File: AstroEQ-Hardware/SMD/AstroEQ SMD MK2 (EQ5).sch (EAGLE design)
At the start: 41 parts, among them IC1 ATMEGA162-16AU, IC2 PIC18F14K50-I/SS, IC3 78L05, J1 POWER_JACKPANEL, M1 Motor Driver, M2 Motor Driver, SW1 SWITCH, X1 16MHz, X2 12MHz

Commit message: Correct Board-Schematic Inconsistencies
In the SMD design, the board and schematic files in Eagle had become
inconsistent. This has been corrected.
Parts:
- R15: device SmartPrj:R-EU_R0603 -> rcl:R-EU_R0603
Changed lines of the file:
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@@
 <?xml version="1.0" encoding="utf-8"?>
 <!DOCTYPE eagle SYSTEM "eagle.dtd">
-<eagle version="6.2">
+<eagle version="6.6.0">
 <drawing>
 <settings>
@@
 <grid distance="0.1" unitdist="inch" unit="inch" style="lines" multiple="1" display="no" altdistance="0.01" altunitdist="inch" altunit="inch"/>
 <layers>
-<layer number="1" name="Top" color="4" fill="1" visible="no" active="no"/>
-<layer number="2" name="Route2" color="1" fill="3" visible="no" active="no"/>
-<layer number="3" name="Route3" color="4" fill="3" visible="no" active="no"/>
-<layer number="14" name="Route14" color="1" fill="6" visible="no" active="no"/>
-<layer number="15" name="Route15" color="4" fill="6" visible="no" active="no"/>
-<layer number="16" name="Bottom" color="1" fill="1" visible="no" active="no"/>
-<layer number="17" name="Pads" color="2" fill="1" visible="no" active="no"/>
-<layer number="18" name="Vias" color="2" fill="1" visible="no" active="no"/>
-<layer number="19" name="Unrouted" color="6" fill="1" visible="no" active="no"/>
-<layer number="20" name="Dimension" color="15" fill="1" visible="no" active="no"/>
-<layer number="21" name="tPlace" color="7" fill="1" visible="no" active="no"/>
-<layer number="22" name="bPlace" color="7" fill="1" visible="no" active="no"/>
-<layer number="23" name="tOrigins" color="15" fill="1" visible="no" active="no"/>
-<layer number="24" name="bOrigins" color="15" fill="1" visible="no" active="no"/>
-<layer number="25" name="tNames" color="15" fill="1" visible="no" active="no"/>
-<layer number="26" name="bNames" color="7" fill="1" visible="no" active="no"/>
-<layer number="27" name="tValues" color="15" fill="1" visible="no" active="no"/>
-<layer number="28" name="bValues" color="7" fill="1" visible="no" active="no"/>
+<layer number="1" name="Top" color="4" fill="1" visible="yes" active="no"/>
+<layer number="2" name="Route2" color="1" fill="3" visible="yes" active="no"/>
+<layer number="3" name="Route3" color="4" fill="3" visible="yes" active="no"/>
+<layer number="14" name="Route14" color="1" fill="6" visible="yes" active="no"/>
+<layer number="15" name="Route15" color="4" fill="6" visible="yes" active="no"/>
+<layer number="16" name="Bottom" color="1" fill="1" visible="yes" active="no"/>
+<layer number="17" name="Pads" color="2" fill="1" visible="yes" active="no"/>
+<layer number="18" name="Vias" color="2" fill="1" visible="yes" active="no"/>
+<layer number="19" name="Unrouted" color="6" fill="1" visible="yes" active="no"/>
+<layer number="20" name="Dimension" color="15" fill="1" visible="yes" active="no"/>
+<layer number="21" name="tPlace" color="7" fill="1" visible="yes" active="no"/>
+<layer number="22" name="bPlace" color="7" fill="1" visible="yes" active="no"/>
+<layer number="23" name="tOrigins" color="15" fill="1" visible="yes" active="no"/>
+<layer number="24" name="bOrigins" color="15" fill="1" visible="yes" active="no"/>
+<layer number="25" name="tNames" color="15" fill="1" visible="yes" active="no"/>
+<layer number="26" name="bNames" color="7" fill="1" visible="yes" active="no"/>
+<layer number="27" name="tValues" color="15" fill="1" visible="yes" active="no"/>
+<layer number="28" name="bValues" color="7" fill="1" visible="yes" active="no"/>
 <layer number="29" name="tStop" color="7" fill="3" visible="no" active="no"/>
 <layer number="30" name="bStop" color="7" fill="6" visible="no" active="no"/>
@@
 <layer number="35" name="tGlue" color="7" fill="4" visible="no" active="no"/>
 <layer number="36" name="bGlue" color="7" fill="5" visible="no" active="no"/>
-<layer number="37" name="tTest" color="7" fill="1" visible="no" active="no"/>
-<layer number="38" name="bTest" color="7" fill="1" visible="no" active="no"/>
+<layer number="37" name="tTest" color="7" fill="1" visible="yes" active="no"/>
+<layer number="38" name="bTest" color="7" fill="1" visible="yes" active="no"/>
 <layer number="39" name="tKeepout" color="4" fill="11" visible="no" active="no"/>
 <layer number="40" name="bKeepout" color="1" fill="11" visible="no" active="no"/>
@@
 <layer number="44" name="Drills" color="15" fill="1" visible="no" active="no"/>
 <layer number="45" name="Holes" color="15" fill="1" visible="no" active="no"/>
-<layer number="46" name="Milling" color="3" fill="1" visible="no" active="no"/>
-<layer number="47" name="Measures" color="7" fill="1" visible="no" active="no"/>
-<layer number="48" name="Document" color="7" fill="1" visible="no" active="no"/>
-<layer number="49" name="Reference" color="7" fill="1" visible="no" active="no"/>
-<layer number="50" name="dxf" color="7" fill="1" visible="no" active="no"/>
-<layer number="51" name="tDocu" color="7" fill="1" visible="no" active="no"/>
-<layer number="52" name="bDocu" color="7" fill="1" visible="no" active="no"/>
-<layer number="53" name="tGND_GNDA" color="7" fill="9" visible="no" active="no"/>
-<layer number="54" name="bGND_GNDA" color="1" fill="9" visible="no" active="no"/>
-<layer number="56" name="wert" color="7" fill="1" visible="no" active="no"/>
+<layer number="46" name="Milling" color="3" fill="1" visible="yes" active="no"/>
+<layer number="47" name="Measures" color="7" fill="1" visible="yes" active="no"/>
+<layer number="48" name="Document" color="7" fill="1" visible="yes" active="no"/>
+<layer number="49" name="Reference" color="7" fill="1" visible="yes" active="no"/>
+<layer number="50" name="dxf" color="7" fill="1" visible="yes" active="no"/>
+<layer number="51" name="tDocu" color="7" fill="1" visible="yes" active="no"/>
+<layer number="52" name="bDocu" color="7" fill="1" visible="yes" active="no"/>
+<layer number="53" name="tGND_GNDA" color="7" fill="9" visible="yes" active="no"/>
+<layer number="54" name="bGND_GNDA" color="1" fill="9" visible="yes" active="no"/>
+<layer number="56" name="wert" color="7" fill="1" visible="yes" active="no"/>
 <layer number="91" name="Nets" color="2" fill="1" visible="yes" active="yes"/>
 <layer number="92" name="Busses" color="1" fill="1" visible="yes" active="yes"/>
@@
 <attribute name="OC_FARNELL" value="1828894"/>
 </part>
-<part name="R15" library="SmartPrj" deviceset="R-EU_" device="R0603" value="1k">
+<part name="R15" library="rcl" deviceset="R-EU_" device="R0603" value="1k">
 <attribute name="MF" value="PANASONIC"/>
 <attribute name="MPN" value="ERJ3GEYJ102V"/>
@@
 </sheet>
 </sheets>
-<errors>
-</errors>
 </schematic>
 </drawing>

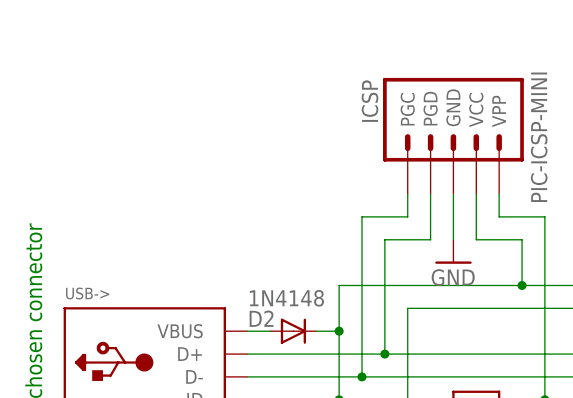
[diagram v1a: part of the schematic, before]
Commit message: Update PCB Logo
Add AstroEQ logo to PCB hardware designs.
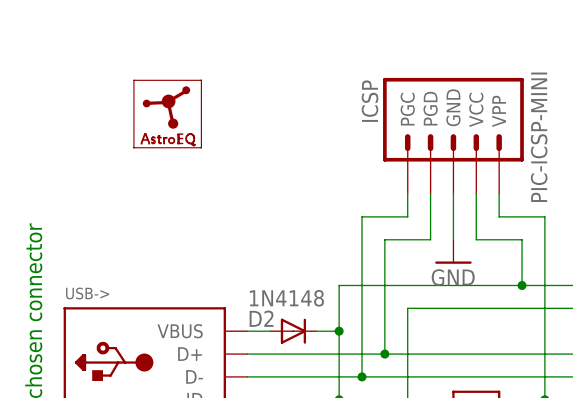
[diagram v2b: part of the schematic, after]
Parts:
- added LOGO1: ASTROEQ5MM, AstroEQTooth:ASTROEQ5MM
- R15: device rcl:R-EU_R0603 -> SmartPrj:R-EU_R0603
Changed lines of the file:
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@@
 <layer number="110" name="fp0" color="7" fill="1" visible="no" active="yes"/>
 <layer number="111" name="LPC17xx" color="7" fill="1" visible="yes" active="yes"/>
+<layer number="112" name="tSilk" color="7" fill="1" visible="no" active="yes"/>
 <layer number="116" name="Patch_BOT" color="9" fill="4" visible="no" active="yes"/>
 <layer number="121" name="_tsilk" color="7" fill="1" visible="no" active="yes"/>
@@
 <layer number="124" name="bTestmark" color="7" fill="1" visible="no" active="yes"/>
 <layer number="125" name="_tNames" color="7" fill="1" visible="no" active="yes"/>
+<layer number="126" name="_bNames" color="7" fill="1" visible="no" active="yes"/>
+<layer number="127" name="_tValues" color="7" fill="1" visible="no" active="yes"/>
+<layer number="128" name="_bValues" color="7" fill="1" visible="no" active="yes"/>
 <layer number="131" name="tAdjust" color="7" fill="1" visible="no" active="yes"/>
 <layer number="132" name="bAdjust" color="7" fill="1" visible="no" active="yes"/>
 <layer number="144" name="Drill_legend" color="7" fill="1" visible="no" active="yes"/>
 <layer number="151" name="HeatSink" color="7" fill="1" visible="no" active="yes"/>
+<layer number="152" name="_bDocu" color="7" fill="1" visible="no" active="yes"/>
 <layer number="199" name="Contour" color="7" fill="1" visible="yes" active="yes"/>
 <layer number="200" name="200bmp" color="1" fill="10" visible="no" active="yes"/>
@@
 <layer number="223" name="223bmp" color="24" fill="1" visible="no" active="no"/>
 <layer number="224" name="224bmp" color="25" fill="1" visible="no" active="no"/>
+<layer number="248" name="Housing" color="7" fill="1" visible="no" active="yes"/>
+<layer number="249" name="Edge" color="7" fill="1" visible="no" active="yes"/>
 <layer number="250" name="Descript" color="3" fill="1" visible="no" active="no"/>
 <layer number="251" name="SMDround" color="12" fill="11" visible="no" active="no"/>
@@
 <attribute name="OC_FARNELL" value="1828894"/>
 </part>
-<part name="R15" library="rcl" deviceset="R-EU_" device="R0603" value="1k">
+<part name="R15" library="SmartPrj" deviceset="R-EU_" device="R0603" value="1k">
 <attribute name="MF" value="PANASONIC"/>
 <attribute name="MPN" value="ERJ3GEYJ102V"/>
@@
 <attribute name="OC_FARNELL" value="1813654"/>
 </part>
+<part name="LOGO1" library="AstroEQTooth" deviceset="ASTROEQ" device="5MM" value="ASTROEQ5MM"/>
 </parts>
 <sheets>
@@
 <attribute name="MPN" x="45.72" y="35.56" size="1.778" layer="96" display="off"/>
 </instance>
+<instance part="LOGO1" gate="G$1" x="5.08" y="116.84"/>
 </instances>
 <busses>
